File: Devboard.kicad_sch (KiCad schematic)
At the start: 33 parts, among them J1 USB_C_Receptacle_USB2.0_14P, J2 Conn_01x20, J3 Conn_01x20, J4 Conn_01x03, SW1 SW_Push, U1 RP2040, U2 NCP1117-3.3_SOT223, U3 W25Q128JVS, Y1 12 MHz

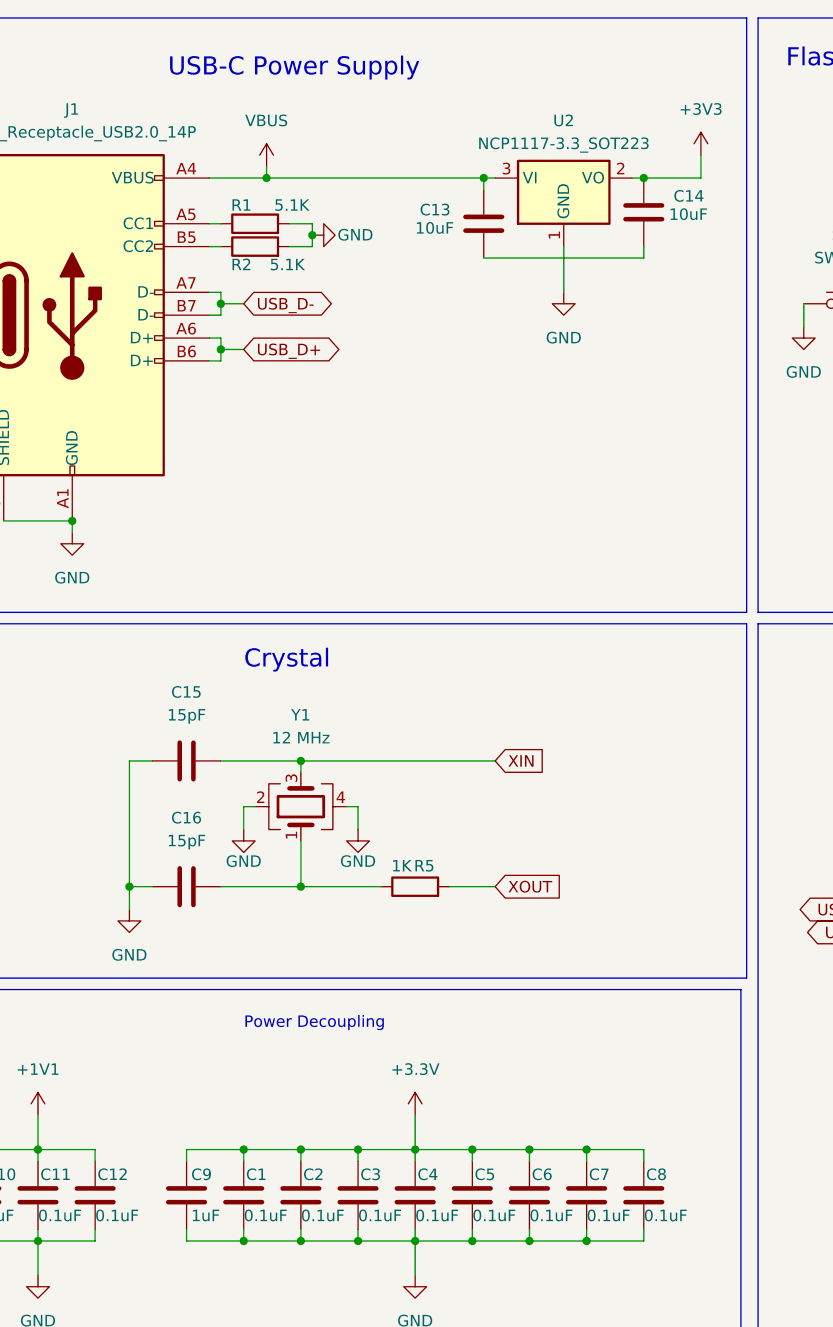
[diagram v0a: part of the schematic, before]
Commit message: Finished routing the PCB
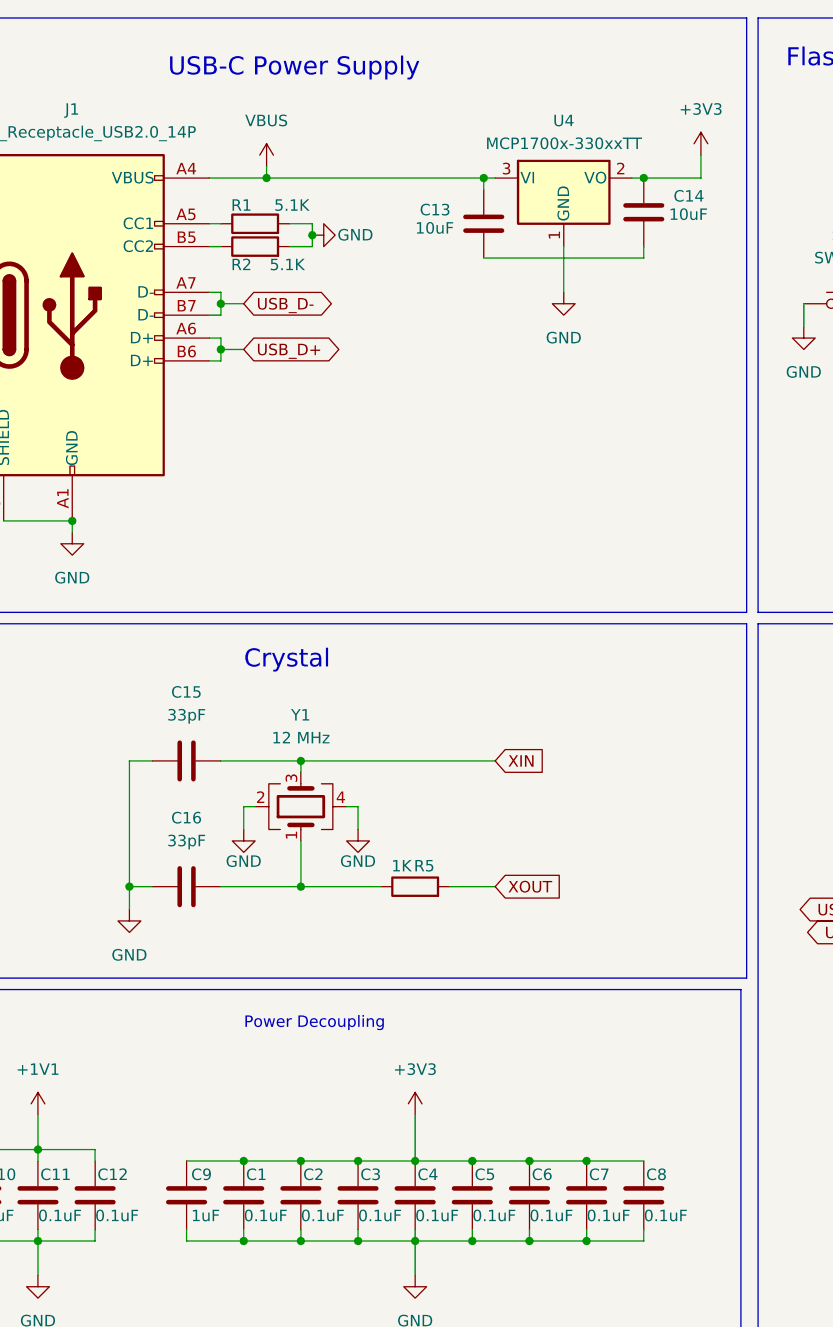
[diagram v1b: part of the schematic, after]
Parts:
- removed U2: NCP1117-3.3_SOT223, Package_TO_SOT_SMD:SOT-223-3_TabPin2, symbol Regulator_Linear:NCP1117-3.3_SOT223
- added U4: MCP1700x-330xxTT, Package_TO_SOT_SMD:SOT-23, symbol Regulator_Linear:MCP1700x-330xxTT
- C1, C10, C11, C12, C17, C2, C3, C4, C5, C6, C7, C8, C9: footprint (none) -> Capacitor_SMD:C_0402_1005Metric
- C13, C14: footprint (none) -> Capacitor_SMD:C_0603_1608Metric
- C15, C16: value 15pF -> 33pF; footprint (none) -> Capacitor_SMD:C_0603_1608Metric
- J1: footprint (none) -> Connector_USB:USB_C_Receptacle_HRO_TYPE-C-31-M-12
- J2, J3: footprint (none) -> Connector_PinHeader_2.54mm:PinHeader_1x20_P2.54mm_Vertical
- J4: footprint (none) -> Connector_PinHeader_2.54mm:PinHeader_1x03_P2.54mm_Vertical
- R1, R2, R3, R4, R5, R6, R7: footprint (none) -> Resistor_SMD:R_0402_1005Metric
- SW1: footprint (none) -> Button_Switch_SMD:SW_Push_SPST_NO_Alps_SKRK
- Y1: footprint (none) -> Crystal:Crystal_SMD_3225-4Pin_3.2x2.5mm
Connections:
- net +3.3V is gone; now on net +3V3: C1.1, C2.1, C3.1, C4.1, C5.1, C6.1, C7.1, C8.1, C9.1
- net +3V3: now also U4.2 (VO)
- net GND: now also U4.1 (GND)
- net VBUS: now also U4.3 (VI)
